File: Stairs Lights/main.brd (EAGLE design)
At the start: 64.4 x 49.5 mm, 45 parts, among them IC1 74LS595N, IC2 74LS595N, Q1 2N7000, Q10 2N7000, Q11 2N7000, Q12 2N7000, Q13 2N7000, Q14 2N7000, Q15 2N7000, Q16 2N7000, Q2 2N7000, Q3 2N7000, Q4 2N7000, Q5 2N7000, Q6 2N7000, Q7 2N7000, Q8 2N7000, Q9 2N7000

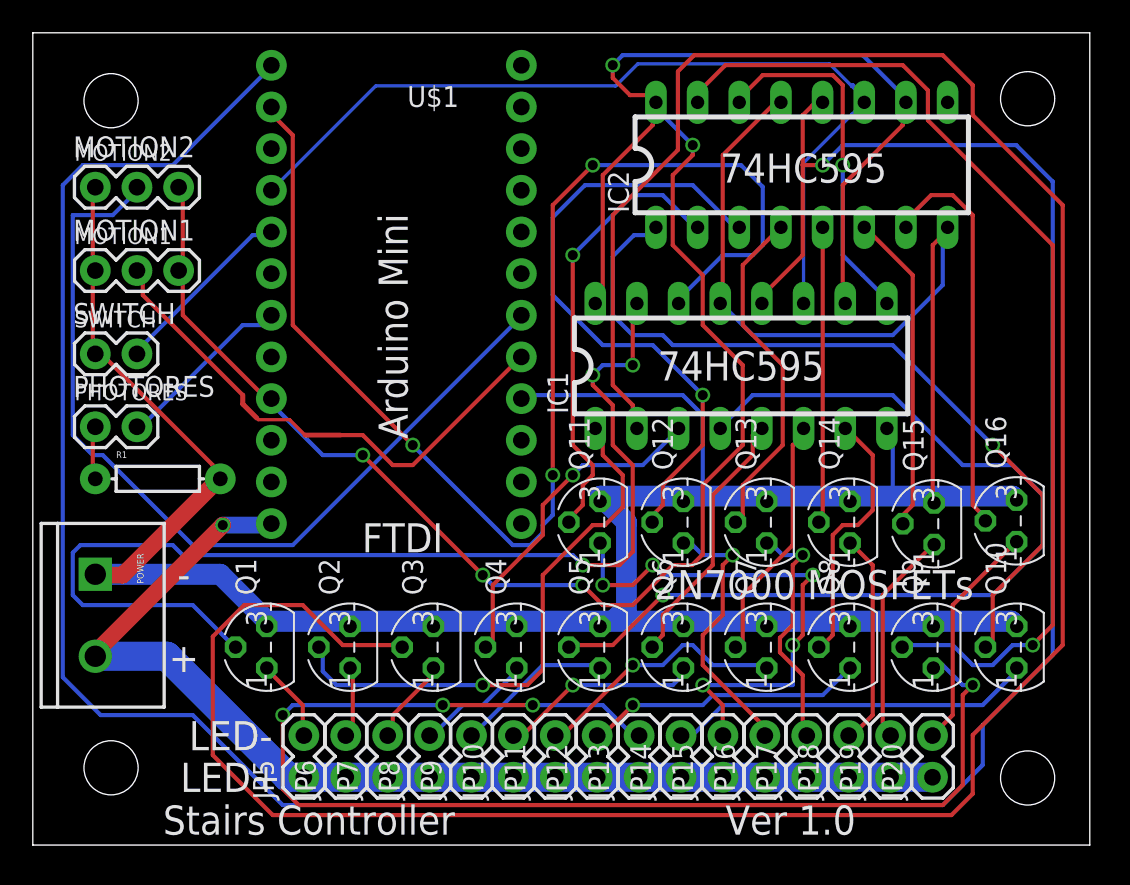
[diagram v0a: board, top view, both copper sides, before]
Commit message: Changed PCB to V1.1, fixed backwards transistor problem
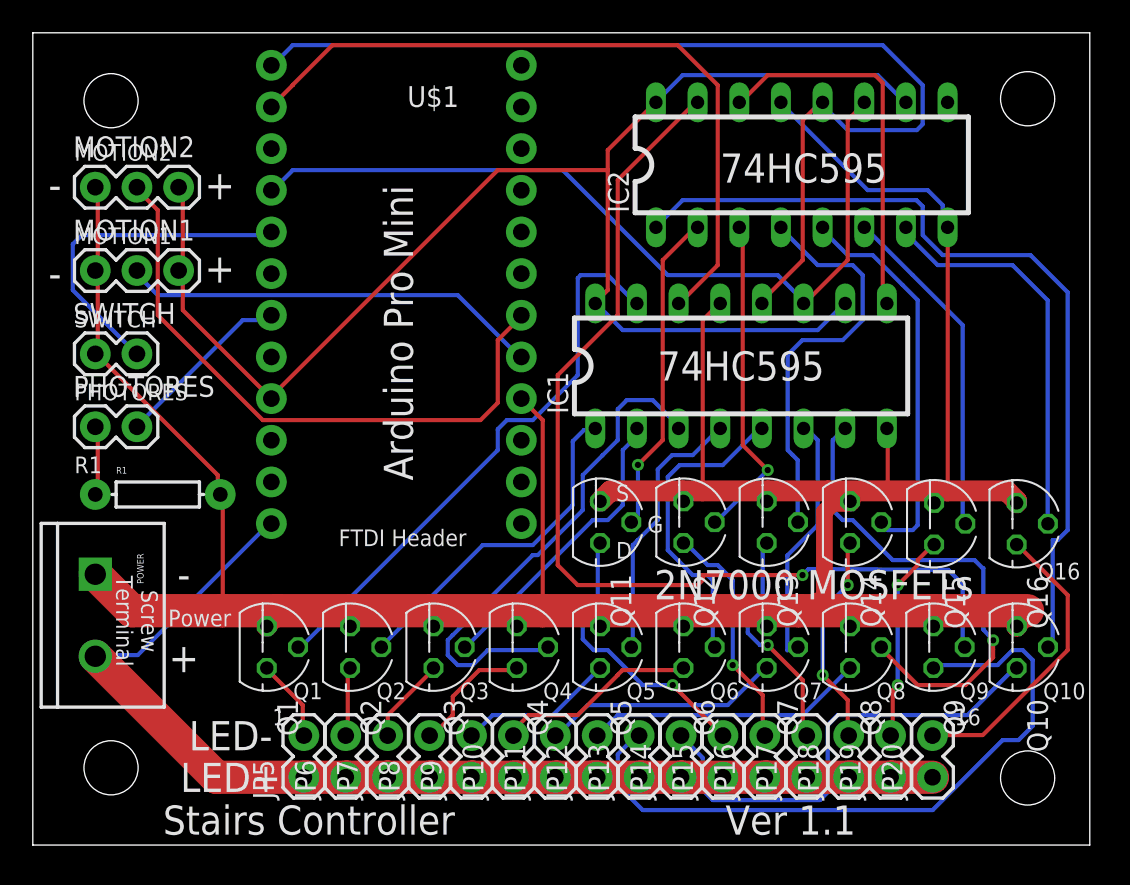
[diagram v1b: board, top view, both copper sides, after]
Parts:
- moved R1 0.95 mm to (7.62, 21.4)
- moved Q16 0.18 mm to (60.0, 19.6), turned to 270 degrees
- turned Q1 to 270 degrees
- turned Q10 to 270 degrees
- turned Q11 to 270 degrees
- turned Q12 to 270 degrees
- turned Q13 to 270 degrees
- turned Q14 to 270 degrees
- turned Q15 to 270 degrees
- turned Q2 to 270 degrees
- turned Q3 to 270 degrees
- turned Q4 to 270 degrees
- turned Q5 to 270 degrees
- turned Q6 to 270 degrees
- turned Q7 to 270 degrees
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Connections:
- net GND: now also Q1.1, Q10.1, Q11.1, Q12.1, Q13.1, Q14.1, Q15.1, Q16.1, Q2.1, Q3.1, Q4.1, Q5.1, Q6.1, Q7.1, Q8.1, Q9.1; no longer Q1.3, Q10.3, Q11.3, Q12.3, Q13.3, Q14.3, Q15.3, Q16.3, Q2.3, Q3.3, Q4.3, Q5.3, Q6.3, Q7.3, Q8.3, Q9.3
- net N$10: now also Q8.3; no longer Q8.1
- net N$11: now also Q9.3; no longer Q9.1
- net N$12: now also Q10.3; no longer Q10.1
- net N$13: now also Q11.3; no longer Q11.1
- net N$14: now also Q12.3; no longer Q12.1
- net N$15: now also Q13.3; no longer Q13.1
- net N$16: now also Q14.3; no longer Q14.1
- net N$17: now also Q16.3; no longer Q16.1
- net N$18: now also Q15.3; no longer Q15.1
- net N$3: now also Q1.3; no longer Q1.1
- net N$4: now also Q2.3; no longer Q2.1
- net N$5: now also Q3.3; no longer Q3.1
- net N$6: now also Q4.3; no longer Q4.1
- net N$7: now also Q5.3; no longer Q5.1
- net N$8: now also Q6.3; no longer Q6.1
- net N$9: now also Q7.3; no longer Q7.1
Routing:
- net LEDCTRL3: track 159.9 -> 18.3 mm
- net SS: track 174.1 -> 64.5 mm, vias 1 -> 0
- net GND: track 284.1 -> 194.6 mm
- net VCC: track 131.6 -> 88.9 mm, vias 5 -> 0
- net LEDCTRL5: track 57.5 -> 16.3 mm, vias 1 -> 0
- net N$11: track 78.9 -> 42.5 mm, vias 4 -> 0
- net MOSI: track 79.8 -> 44.1 mm, vias 3 -> 0
- net LEDCTRL1: track 67.4 -> 34.9 mm, vias 3 -> 0
- net LEDCTRL12: track 38.6 -> 20.1 mm
- net MOTION2: track 54.1 -> 38.0 mm
- net N$13: track 32.5 -> 17.5 mm, vias 5 -> 1
- net LEDCTRL8: track 16.0 -> 30.1 mm, vias 0 -> 1
- net LEDCTRL2: track 33.5 -> 20.8 mm, vias 1 -> 0
- net LEDCTRL4: track 20.5 -> 31.1 mm, vias 1 -> 0
- net SWITCH_PIN: track 11.3 -> 20.7 mm
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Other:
- board text added: "1"
- board text added: "16"
- board text added: "Arduino Pro Mini"
- board text added: "D"
- board text added: "FTDI Header"
- board text added: "G"
- board text added: "Power"
- board text added: "Q1"
- board text added: "Q10"
- board text added: "Q16"
- board text added: "Q2"
- board text added: "Q3"
- board text added: "Q4"
- board text added: "Q5"
- board text added: "Q6"
- board text added: "Q7"
- board text added: "Q8"
- board text added: "Q9"
- board text added: "R1"
- board text added: "S"
- board text added: "Screw Terminal"
- board text added: "Ver 1.1"
- board text removed: "Arduino Mini"
- board text removed: "FTDI"
- board text removed: "Ver 1.0"

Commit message: Updated to version 1.2
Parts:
- added C1, C2: (no value), SparkFun:CAP-PTH-SMALL-KIT
- added IC3: (no value), SparkFun:TO220-IGO
- moved IC1 9.21 mm to (52.4, 29.2)
- moved IC2 1.00 mm to (46.6, 42.4)
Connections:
- net 12V: now also C1.1, IC3.IN
- net GND: now also C1.2, C2.2, IC3.GND
- net VCC: now also C2.1, IC3.OUT
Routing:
- net LEDCTRL2: track 20.8 -> 106.3 mm, vias 0 -> 1
- net 12V: track 72.7 -> 107.4 mm
- net LEDCTRL12: track 20.1 -> 41.5 mm, vias 1 -> 0
- net GND: track 194.6 -> 209.2 mm
- net LEDCTRL8: track 30.1 -> 39.8 mm
- net SCK: track 50.2 -> 59.6 mm
- net LEDCTRL9: track 61.8 -> 52.6 mm, vias 1 -> 2
- net N$2: track 23.2 -> 32.4 mm, vias 0 -> 1
- net LEDCTRL1: track 34.9 -> 43.9 mm
- net LEDCTRL3: track 18.3 -> 27.1 mm
- net VCC: track 88.9 -> 97.7 mm
- net LEDCTRL4: track 31.1 -> 39.4 mm
- net LEDCTRL5: track 16.3 -> 23.7 mm
- net LEDCTRL6: track 19.0 -> 25.9 mm, vias 0 -> 3
- net LEDCTRL7: track 15.4 -> 20.4 mm, vias 0 -> 1
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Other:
- board text added: "7805 Regulator"
- board text added: "C1"
- board text added: "C2"
- board text added: "Ver 1.2"
- board text removed: "Ver 1.1"

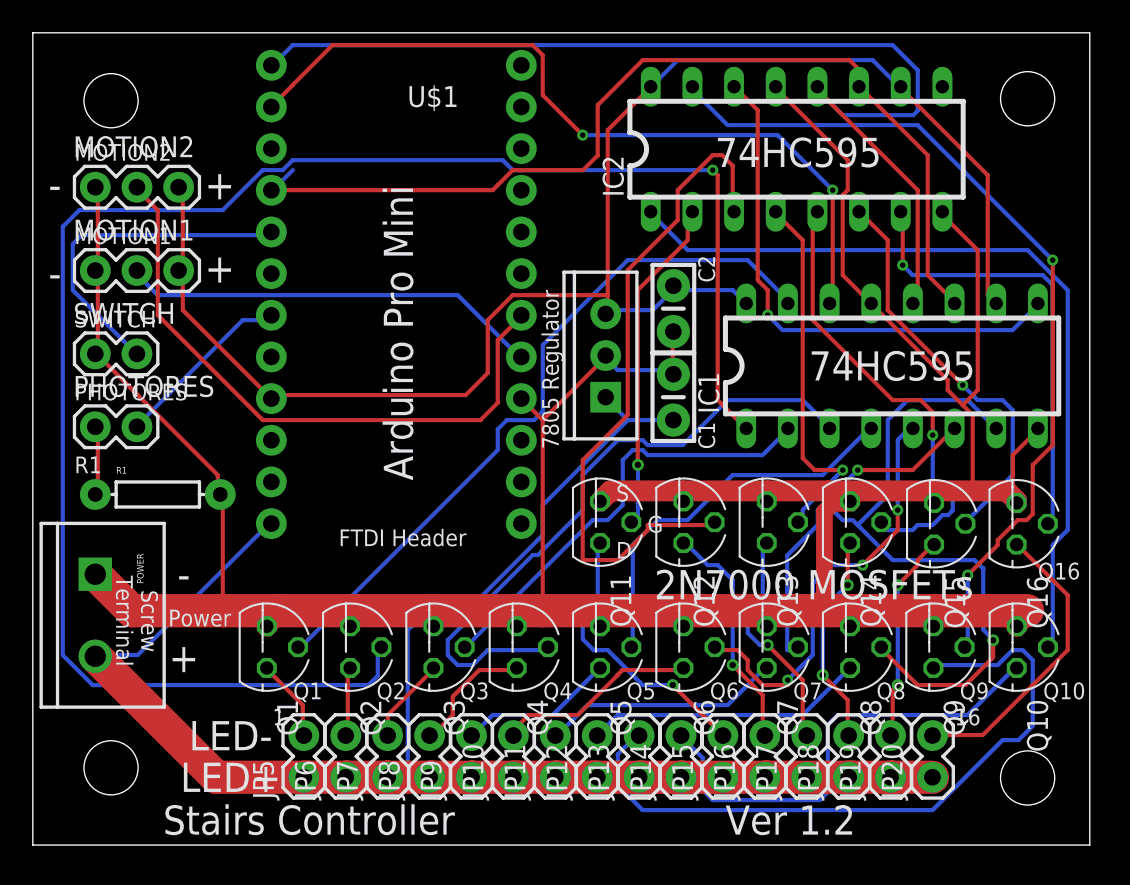
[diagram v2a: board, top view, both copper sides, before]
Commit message: 1.3 Fixed photoresistor hardware problem
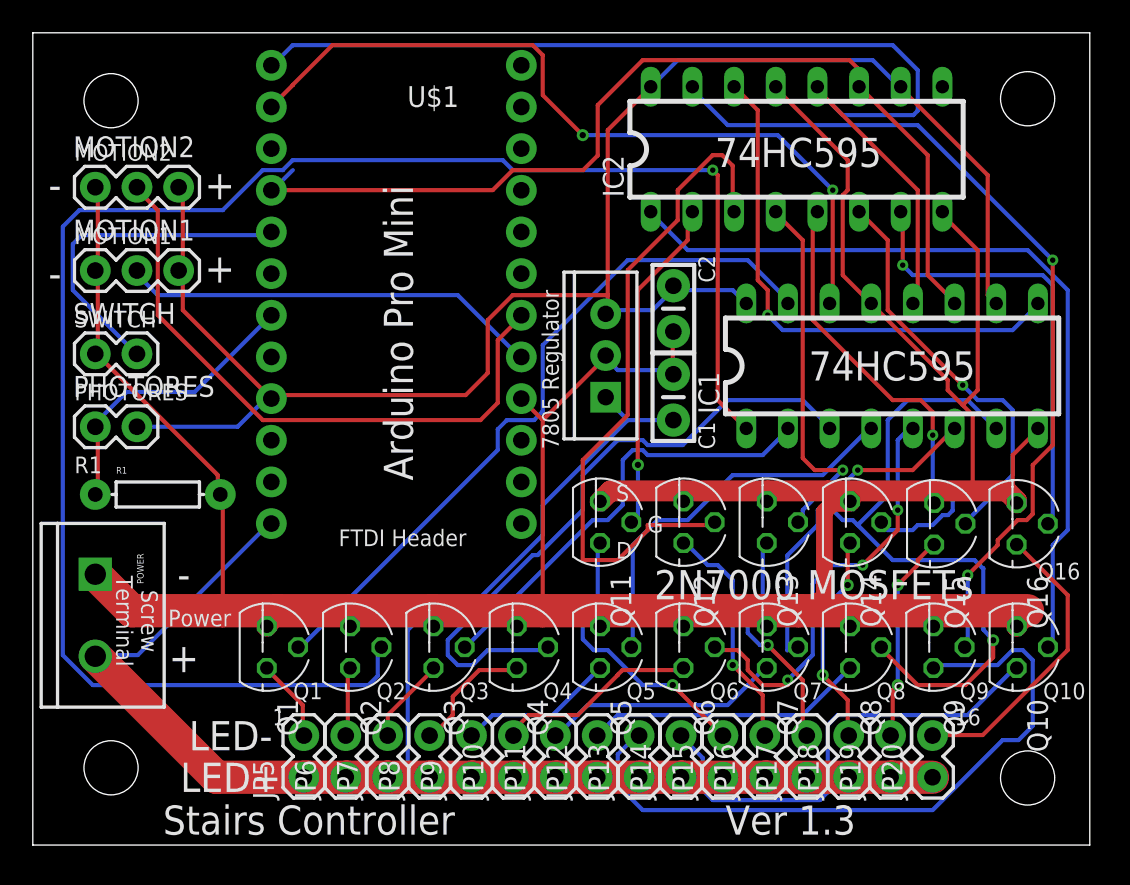
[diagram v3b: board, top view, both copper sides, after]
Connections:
- removed net N$22: PHOTORES.1, R1.P$1
- net PHOTORESIST_PIN: now also PHOTORES.1, R1.P$1; no longer PHOTORES.2
- net VCC: now also PHOTORES.2
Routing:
- net VCC: track 97.7 -> 106.5 mm
- net PHOTORESIST_PIN: track 11.1 -> 18.0 mm
- net N$22: track 4.22 -> 0.00 mm
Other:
- board text added: "Ver 1.3"
- board text removed: "Ver 1.2"
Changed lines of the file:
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@@
 <?xml version="1.0" encoding="utf-8"?>
 <!DOCTYPE eagle SYSTEM "eagle.dtd">
-<eagle version="6.5.0">
+<eagle version="7.3.0">
 <drawing>
 <settings>
@@
 <wire x1="0" y1="49.52" x2="0" y2="0" width="0" layer="20"/>
 <text x="7.9375" y="0.635" size="1.778" layer="121" font="vector">Stairs Controller</text>
-<text x="42.2275" y="0.635" size="1.778" layer="121" font="vector">Ver 1.2</text>
+<text x="42.2275" y="0.635" size="1.778" layer="121" font="vector">Ver 1.3</text>
 <text x="23.1775" y="22.225" size="1.778" layer="121" font="vector" rot="R90">Arduino Pro Mini</text>
 <text x="46.6725" y="42.2275" size="1.778" layer="121" font="vector" align="center">74HC595</text>
@@
 <autorouter>
 <pass name="Default">
-<param name="RoutingGrid" value="12mil"/>
+<param name="RoutingGrid" value="12.5mil"/>
+<param name="AutoGrid" value="1"/>
+<param name="Efforts" value="0"/>
+<param name="TopRouterVariant" value="1"/>
 <param name="tpViaShape" value="round"/>
 <param name="PrefDir.1" value="|"/>
@@
 <wire x1="35.052" y1="33.528" x2="29.2608" y2="33.528" width="0.254" layer="1"/>
 <wire x1="14.6304" y1="27.432" x2="14.5438" y2="27.2184" width="0.254" layer="1"/>
+<contactref element="PHOTORES" pad="2"/>
+<wire x1="6.35" y1="25.5016" x2="12.48233125" y2="25.5016" width="0.254" layer="16"/>
+<wire x1="12.48233125" y1="25.5016" x2="14.36963125" y2="27.3889" width="0.254" layer="16"/>
+<wire x1="14.36963125" y1="27.3889" x2="14.3256" y2="27.432" width="0" layer="19" extent="1-16"/>
 </signal>
 <signal name="GND">
@@
 <wire x1="48.768" y1="33.2232" x2="48.5775" y2="33.02" width="0.254" layer="1"/>
 <via x="48.768" y="39.9288" extent="1-16" drill="0.3302"/>
-<via x="33.528" y="43.2816" extent="1-16" drill="0.3302"/>
+<via x="33.528" y="43.2816" extent="1-16" drill="0.381"/>
 </signal>
 <signal name="SCK">
@@
 <wire x1="56.0832" y1="33.2232" x2="56.1975" y2="33.02" width="0.254" layer="1"/>
 <wire x1="50.5968" y1="46.0248" x2="50.3725" y2="46.2325" width="0.254" layer="1"/>
-<wire x1="28.3464" y1="40.2336" x2="28.0416" y2="39.9288" width="0.254" layer="1"/>
 <wire x1="28.0416" y1="39.9288" x2="14.6304" y2="39.9288" width="0.254" layer="1"/>
-<wire x1="29.2608" y1="41.148" x2="28.3464" y2="40.2336" width="0.254" layer="1"/>
+<wire x1="29.2608" y1="41.148" x2="28.0416" y2="39.9288" width="0.254" layer="1"/>
 <wire x1="34.4424" y1="45.1104" x2="34.4424" y2="42.043234375" width="0.254" layer="1"/>
 <wire x1="34.4424" y1="42.043234375" x2="33.547165625" y2="41.148" width="0.254" layer="1"/>
@@
 <wire x1="35.052" y1="27.1272" x2="34.925" y2="27.305" width="0.254" layer="16"/>
 <wire x1="31.0896" y1="20.7264" x2="36.2712" y2="25.908" width="0.254" layer="16"/>
-<wire x1="30.7848" y1="18.5928" x2="31.0896" y2="18.8976" width="0.254" layer="16"/>
 <wire x1="31.0896" y1="18.8976" x2="31.0896" y2="20.7264" width="0.254" layer="16"/>
-<wire x1="26.5176" y1="14.3256" x2="30.7848" y2="18.5928" width="0.254" layer="16"/>
+<wire x1="26.5176" y1="14.3256" x2="31.0896" y2="18.8976" width="0.254" layer="16"/>
 <wire x1="24.0792" y1="14.3256" x2="26.5176" y2="14.3256" width="0.254" layer="16"/>
 <wire x1="22.86" y1="13.1064" x2="24.0792" y2="14.3256" width="0.254" layer="16"/>
@@
 <wire x1="53.34" y1="27.1272" x2="56.9976" y2="27.1272" width="0.254" layer="16"/>
 <wire x1="52.1208" y1="25.908" x2="53.34" y2="27.1272" width="0.254" layer="16"/>
-<wire x1="51.5112" y1="20.7264" x2="52.1208" y2="21.336" width="0.254" layer="16"/>
 <wire x1="52.1208" y1="21.336" x2="52.1208" y2="25.908" width="0.254" layer="16"/>
-<wire x1="50.292" y1="19.5072" x2="51.5112" y2="20.7264" width="0.254" layer="16"/>
+<wire x1="50.292" y1="19.5072" x2="52.1208" y2="21.336" width="0.254" layer="16"/>
 <wire x1="58.5216" y1="25.6032" x2="58.7375" y2="25.4" width="0.254" layer="16"/>
 </signal>
@@
 <contactref element="IC2" pad="1"/>
 <contactref element="Q10" pad="2"/>
-<wire x1="62.484" y1="18.5928" x2="62.1792" y2="18.288" width="0.254" layer="16"/>
 <wire x1="62.1792" y1="18.288" x2="62.1792" y2="12.192" width="0.254" layer="16"/>
-<wire x1="63.0936" y1="19.2024" x2="62.484" y2="18.5928" width="0.254" layer="16"/>
+<wire x1="63.0936" y1="19.2024" x2="62.1792" y2="18.288" width="0.254" layer="16"/>
 <wire x1="62.1792" y1="12.192" x2="61.89" y2="12.065" width="0.254" layer="16"/>
 <wire x1="39.9288" y1="36.2712" x2="37.7952" y2="38.4048" width="0.254" layer="16"/>
@@
 <contactref element="IC2" pad="4"/>
 <contactref element="Q13" pad="2"/>
-<wire x1="48.4632" y1="21.9456" x2="46.9392" y2="20.4216" width="0.254" layer="16"/>
+<wire x1="49.3776" y1="22.86" x2="46.9392" y2="20.4216" width="0.254" layer="16"/>
 <wire x1="46.9392" y1="20.4216" x2="46.9392" y2="19.812" width="0.254" layer="16"/>
-<wire x1="49.3776" y1="22.86" x2="48.4632" y2="21.9456" width="0.254" layer="16"/>
 <wire x1="46.9392" y1="36.8808" x2="46.9392" y2="23.594075" width="0.254" layer="1"/>
 <wire x1="46.9392" y1="23.594075" x2="47.673275" y2="22.86" width="0.254" layer="1"/>
@@
 <contactref element="JP15" pad="2"/>
 <contactref element="Q11" pad="3"/>
-<wire x1="34.1376" y1="14.3256" x2="34.4424" y2="14.6304" width="0.254" layer="16"/>
 <wire x1="34.4424" y1="14.6304" x2="34.4424" y2="18.288" width="0.254" layer="16"/>
-<wire x1="33.528" y1="13.716" x2="34.1376" y2="14.3256" width="0.254" layer="16"/>
+<wire x1="33.528" y1="13.716" x2="34.4424" y2="14.6304" width="0.254" layer="16"/>
 <wire x1="35.052" y1="11.8872" x2="34.19350625" y2="11.8872" width="0.254" layer="16"/>
 <wire x1="34.19350625" y1="11.8872" x2="33.528" y2="12.55270625" width="0.254" layer="16"/>
@@
 <wire x1="59.1312" y1="27.1272" x2="57.6072" y2="27.1272" width="0.254" layer="16"/>
 <wire x1="59.7408" y1="26.5176" x2="59.1312" y2="27.1272" width="0.254" layer="16"/>
-<wire x1="59.1312" y1="21.9456" x2="59.7408" y2="22.5552" width="0.254" layer="16"/>
 <wire x1="59.7408" y1="22.5552" x2="59.7408" y2="26.5176" width="0.254" layer="16"/>
-<wire x1="56.9976" y1="19.812" x2="59.1312" y2="21.9456" width="0.254" layer="16"/>
+<wire x1="56.9976" y1="19.812" x2="59.7408" y2="22.5552" width="0.254" layer="16"/>
 <wire x1="50.5968" y1="38.4048" x2="50.3725" y2="38.6125" width="0.254" layer="1"/>
 <wire x1="56.9976" y1="19.812" x2="56.855" y2="19.59" width="0.254" layer="16"/>
@@
 <wire x1="14.3256" y1="37.1856" x2="14.5438" y2="37.3784" width="0.254" layer="16"/>
 </signal>
-<signal name="N$22">
+<signal name="PHOTORESIST_PIN">
+<contactref element="U$1" pad="19"/>
 <contactref element="PHOTORES" pad="1"/>
 <contactref element="R1" pad="P$1"/>
@@
 <wire x1="3.9624" y1="21.6408" x2="3.81" y2="21.3741" width="0.254" layer="1"/>
 <wire x1="3.9624" y1="25.2984" x2="3.81" y2="25.5016" width="0.254" layer="1"/>
-</signal>
-<signal name="PHOTORESIST_PIN">
-<contactref element="PHOTORES" pad="2"/>
-<contactref element="U$1" pad="19"/>
-<wire x1="12.8016" y1="32.004" x2="6.4008" y2="25.6032" width="0.254" layer="16"/>
-<wire x1="14.3256" y1="32.004" x2="12.8016" y2="32.004" width="0.254" layer="16"/>
-<wire x1="6.4008" y1="25.6032" x2="6.35" y2="25.5016" width="0.254" layer="16"/>
-<wire x1="14.3256" y1="32.004" x2="14.5438" y2="32.2984" width="0.254" layer="16"/>
+<wire x1="3.9624" y1="25.2984" x2="3.9624" y2="25.8699" width="0.254" layer="16"/>
+<wire x1="3.9624" y1="25.8699" x2="5.715" y2="27.6225" width="0.254" layer="16"/>
+<wire x1="5.715" y1="27.6225" x2="9.8679" y2="27.6225" width="0.254" layer="16"/>
+<wire x1="9.8679" y1="27.6225" x2="14.5438" y2="32.2984" width="0.254" layer="16"/>
+<wire x1="3.9624" y1="25.2984" x2="3.9624" y2="25.2984" width="0" layer="19" extent="1-16"/>
 </signal>
 <signal name="MOTION1">
